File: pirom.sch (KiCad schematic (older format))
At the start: 4 parts

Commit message: MORE SCHEMATIC WORK
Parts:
- added U? (x2): 74HC164, symbol 74xx:74HC164
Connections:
- net A14: now reaches U?.1 (A14)
- net A14: now also U?.12 (Q6)
- net A0: now reaches U?.10 (A0)
- net A0: now also U?.3 (Q0)
- net D0: now reaches U?.11 (D0)
- net D0: now also U?.11 (D0), U?.3 (Q0)
- net D1: now reaches U?.12 (D1)
- net D1: now also U?.12 (D1), U?.4 (Q1)
- net D2: now reaches U?.13 (D2)
- net D2: now also U?.13 (D2), U?.5 (Q2)
- net GND: now reaches U?.14 (GND)
- net GND: now also J?.14 (GND), J?.20 (GND), J?.25 (GND), J?.30 (GND), J?.34 (GND), J?.39 (GND), J?.6 (GND), J?.9 (GND), U?.10 (DS), U?.7 (GND), U?.8 (GND), U?.7 (GND), U?.7 (GND)
- net D3: now reaches U?.15 (D3)
- net D3: now also U?.14 (D3), U?.6 (Q3)
- net D4: now reaches U?.16 (D4)
- net D4: now also U?.3 (D4), U?.10 (Q4)
- net D5: now reaches U?.17 (D5)
- net D5: now also U?.4 (D5), U?.11 (Q5)
- net D6: now reaches U?.18 (D6)
- net D6: now also U?.5 (D6), U?.12 (Q6)
- net D7: now reaches U?.19 (D7)
- net D7: now also U?.1 (DSA), U?.2 (DSB), U?.6 (D7), U?.13 (Q7)
- net A12: now reaches U?.2 (A12)
- net A12: now also U?.10 (Q4)
- net A10: now reaches U?.21 (A10)
- net A10: now also U?.5 (Q2)
- net A11: now reaches U?.23 (A11)
- net A11: now also U?.6 (Q3)
- net A9: now reaches U?.24 (A9)
- net A9: now also U?.4 (Q1)
- net A8: now reaches U?.25 (A8)
- net A8: now also U?.3 (Q0)
- net A13: now reaches U?.26 (A13)
- net A13: now also U?.11 (Q5)
- net +5V: now reaches U?.28 (VCC)
- net +5V: now also J?.2 (5V), J?.4 (5V), U?.14 (VCC)
- net A7: now reaches U?.3 (A7)
- net A7: now also U?.13 (Q7), U?.1 (DSA), U?.2 (DSB)
- net A6: now reaches U?.4 (A6)
- net A6: now also U?.12 (Q6)
- net A5: now reaches U?.5 (A5)
- net A5: now also U?.11 (Q5)
- net A4: now reaches U?.6 (A4)
- net A4: now also U?.10 (Q4)
- net A3: now reaches U?.7 (A3)
- net A3: now also U?.6 (Q3)
- net A2: now reaches U?.8 (A2)
- net A2: now also U?.5 (Q2)
- net A1: now reaches U?.9 (A1)
- net A1: now also U?.4 (Q1)
- net +3V3: now reaches J?.1 (3V3)
- net +3V3: now also J?.17 (3V3), U?.16 (VCC), U?.14 (VCC)
- net LOAD_: now reaches J?.15 (GPIO22)
- net LOAD_: now also U?.1 (~PL)
- net MISO: now reaches J?.35 (GPIO19/MISO1)
- net MISO: now also U?.9 (Q7)
- net MOSI: now reaches J?.38 (GPIO20/MOSI1)
- net MOSI: now also U?.1 (DSA), U?.2 (DSB)
- net CLK: now reaches J?.40 (GPIO21/SCLK1)
- net CLK: now also U?.15 (~CE), U?.2 (CP), U?.8 (CP), U?.8 (CP), U?.8 (CP)
- net CLEAR_ADDRESS: now reaches U?.9 (~MR)
- net CLEAR_ADDRESS: now also U?.9 (~MR)
- new net A15: U?.13 (Q7)
- new net CLEAR_DATA: U?.9 (~MR)
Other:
- moved on the sheet: J?, U?

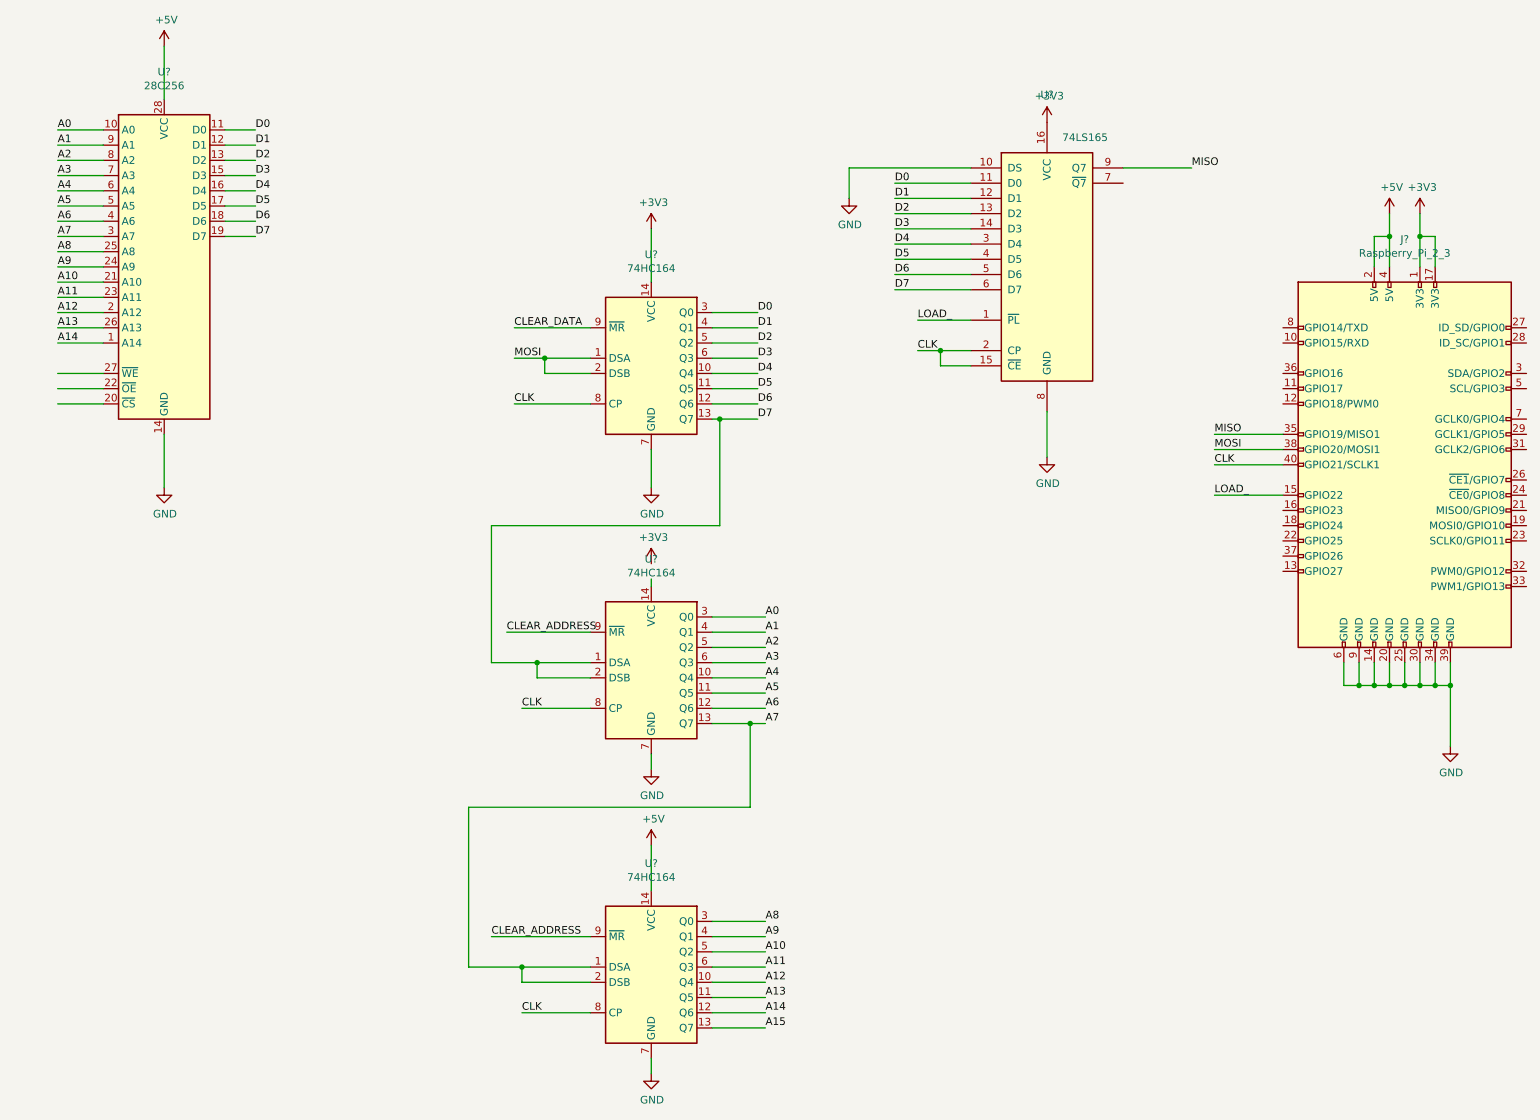
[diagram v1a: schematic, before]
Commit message: schmatic complete needs checking
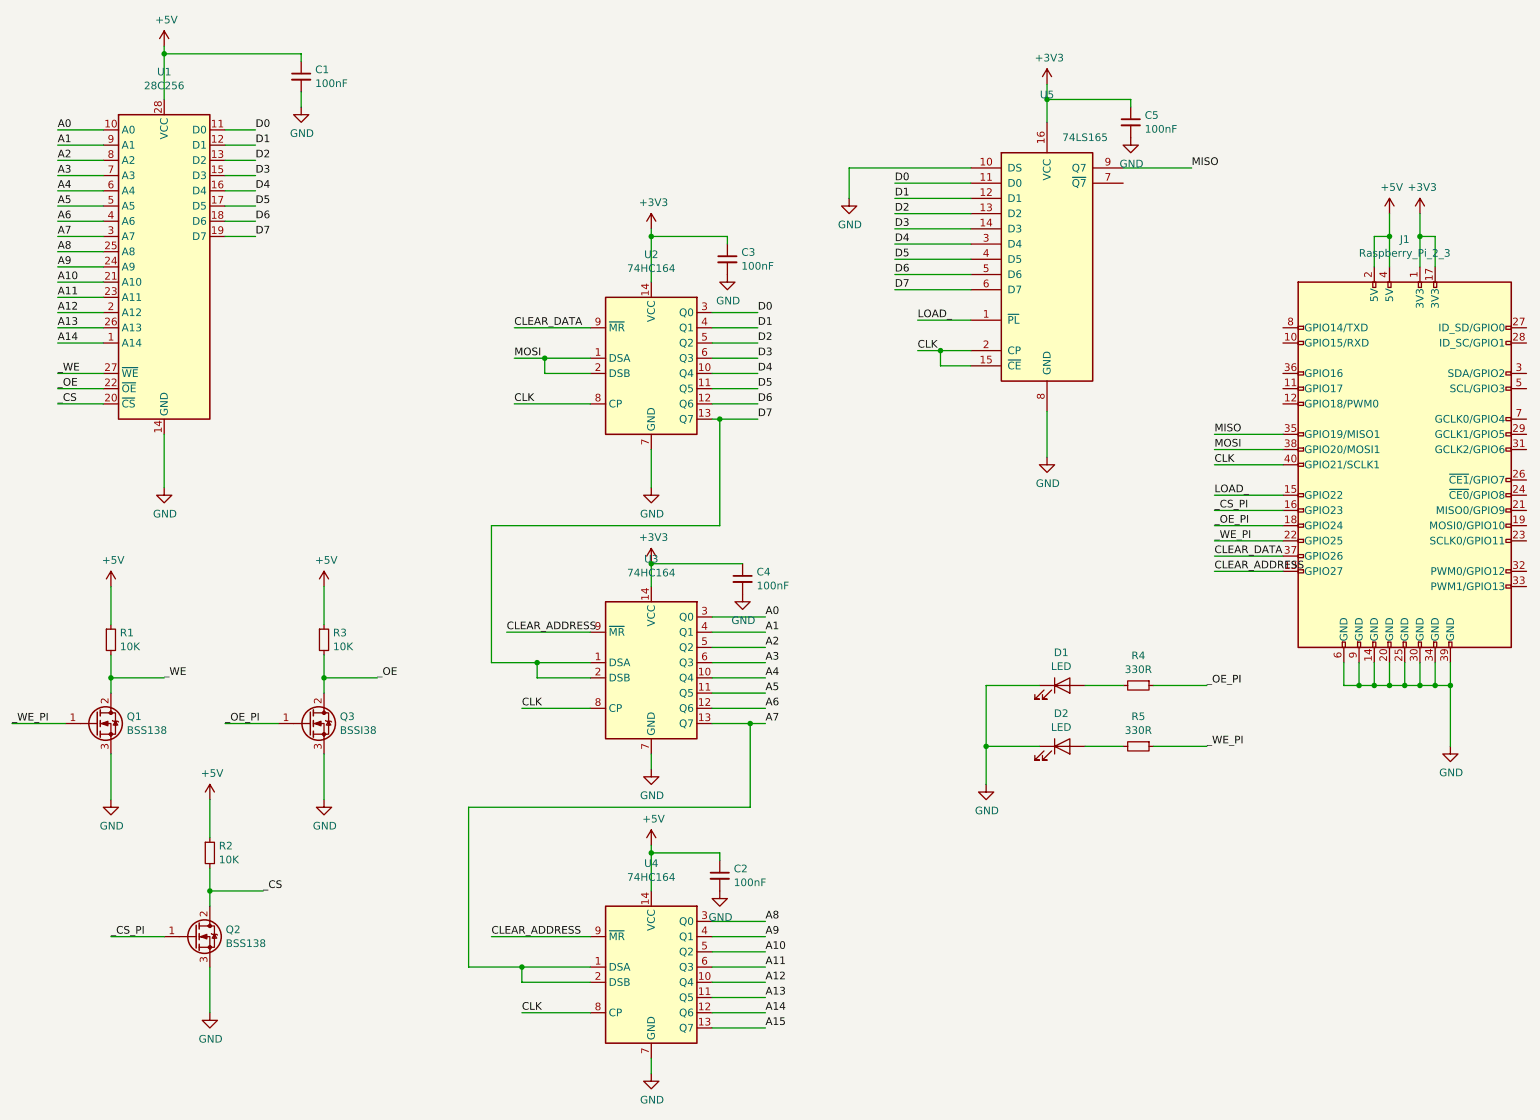
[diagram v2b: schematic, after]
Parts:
- added C1, C2, C3, C4, C5: 100nF, symbol Device:C_Small
- added D1, D2: LED, symbol Device:LED
- added Q1, Q2: BSS138, symbol Device:Q_NMOS_GDS
- added Q3: BSSI38, symbol Device:Q_NMOS_GDS
- added R1, R2, R3: 10K, symbol Device:R_Small
- added R4, R5: 330R, symbol Device:R_Small
- U1: renamed from U?; footprint (none) -> Package_DIP:DIP-28_W15.24mm
- U2, U3, U4, U5: renamed from U?; footprint (none) -> Package_SO:SOIC-14_3.9x8.7mm_P1.27mm
- gave numbers to parts that had none: 1
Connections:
- net +3V3: now also U3.14 (VCC), C3.1, C4.1, C5.1
- net +5V: now also C1.1, C2.1, R1.1, R2.1, R3.1
- net CLEAR_ADDRESS: now also J1.13 (GPIO27)
- net CLEAR_DATA: now also J1.37 (GPIO26)
- net GND: now also C1.2, C2.2, C3.2, C4.2, C5.2, D1.1 (K), D2.1 (K), Q1.3 (S), Q2.3 (S), Q3.3 (S)
- net _CS: now reaches U1.20 (~CS)
- net _CS: now also Q2.2 (D), R2.2
- net _OE: now reaches U1.22 (~OE)
- net _OE: now also Q3.2 (D), R3.2
- net _WE: now reaches U1.27 (~WE)
- net _WE: now also Q1.2 (D), R1.2
- net _CS_PI: now reaches J1.16 (GPIO23)
- net _CS_PI: now also Q2.1 (G)
- net _OE_PI: now reaches J1.18 (GPIO24)
- net _OE_PI: now also Q3.1 (G), R4.1
- net _WE_PI: now reaches J1.22 (GPIO25)
- net _WE_PI: now also Q1.1 (G), R5.1
- new net: D1.2 (A), R4.2
- new net: D2.2 (A), R5.2
